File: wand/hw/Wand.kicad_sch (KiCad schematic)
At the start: 43 parts, among them J2 Conn_01x04, J2 Conn_01x08, J3 Conn_01x08, J4 Conn_01x04, M1 Motor_DC, Q1 Si2301, SW1 SW_SPST, SW2 Vib, U1 SPX3819M5-L-3-3, U2 STM32G030F6Px, U3 BMI270, U4 MMC5603NJ, U5 nRF24L01P, Y1 16MHz

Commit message: (WIP) Wand PCB design
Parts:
- added AE1: 2.4GHz 50R, Wand_footprints:ANT_IFA_USB_2.4GHz_50R, symbol Device:Antenna_Dipole
- added C19, C2: 4.7u, Capacitor_SMD:C_0603_1608Metric, symbol Device:C
- added C20: 10u, Capacitor_SMD:C_0603_1608Metric, symbol Device:C
- added D1: SMBJ5.0A, Diode_SMD:D_SMB, symbol Diode:SMF5V0A
- added D2: LED, LED_SMD:LED_0603_1608Metric, symbol Device:LED
- added J5: USB_C_Receptacle_PowerOnly_6P, Wand_footprints:USB_C_Receptacle, symbol Connector:USB_C_Receptacle_PowerOnly_6P
- added Q1: Si2301, Package_TO_SOT_SMD:SOT-23, symbol Device:Q_NMOS_GSD
- added R10, R3: 1k, Resistor_SMD:R_0603_1608Metric, symbol Device:R
- added R11, R12: 5.1k, Resistor_SMD:R_0603_1608Metric, symbol Device:R
- added R13: 2k, Resistor_SMD:R_0603_1608Metric, symbol Device:R
- added R14: 6.8k, Resistor_SMD:R_0603_1608Metric, symbol Device:R
- added U6: LTC4054ES5-4.2, Package_TO_SOT_SMD:TSOT-23-5, symbol Battery_Management:LTC4054ES5-4.2
- BT1: value LIR2016 -> LiPo
- J4: footprint Connector_PinHeader_2.00mm:PinHeader_1x04_P2.00mm_Vertical -> Connector_PinHeader_1.00mm:PinHeader_1x04_P1.00mm_Vertical
- renumbered C9 to C10, C10 to C11, C11 to C12, C12 to C13, C13 to C14, C14 to C15, C15 to C16, C16 to C17, C17 to C18, C6 to C7, C7 to C8, C8 to C9, Q1 to Q2, R6 to R7, R7 to R8, R8 to R9
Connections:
- net BMI_CS: now also U2.10 (PA3); no longer U2.14 (PA7)
- net GND: now also AE1.2, C19.2, C2.2, C20.2, D1.2 (A2), J5.A12 (GND), J5.B12 (GND), R11.2, R12.2, R13.2, U6.2 (GND)
- net MOTOR_G: now also U2.11 (PA4), R10.1; no longer Q2.1 (G), U2.16 (PA11/PA9)
- net VBAT: now also C20.1, U6.3 (BAT)
- net VDD: now also C2.1, Q1.3 (D); no longer C1.1, C1.1, C7.2, J2.1 (Pin_1), J3.1 (Pin_1), J4.2 (Pin_2), U3.5 (VDDIO), U3.8 (VDD), U4.B1 (VDD)
- net nRF_CE: now also U2.16 (PA11/PA9); no longer U2.11 (PA4)
- net nRF_CS: now also U2.14 (PA7); no longer U2.10 (PA3)
- net at C15.2, C16.1: now also AE1.1
- net SUB_VDD_G: now reaches U2.2 (PC14/PB9)
- net SUB_VDD_G: now also R3.1
- net SPI1_CK renamed SPI1_SCK
- new net: Q1.1 (G), R3.2
- new net: D2.1 (K), U6.1 (~{CHRG})
- new net: D2.2 (A), R14.2
- new net: R13.1, U6.5 (PROG)
- new net: J5.A5 (CC1), R12.1
- new net: J5.B5 (CC2), R11.1
- new net: Q2.1 (G), R10.2
- new net VBUS: C19.1, D1.1 (A1), J5.A9 (VBUS), J5.B9 (VBUS), R14.1, U6.4 (V_{CC})
- new net VDDSUB: C1.1, C1.1, C7.2, J2.1 (Pin_1), J3.1 (Pin_1), J4.2 (Pin_2), Q1.2 (S), U3.5 (VDDIO), U3.8 (VDD), U4.B1 (VDD)
- no-connect marks 10 -> 9
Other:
- note added: "LTH7"
- note added: "P1.0 1x04"
- note removed: "P2.0 1x04"
- moved on the sheet: BT1, C1, C2, C3, C7, J2, J3, J4, R1, R6, R7, R8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

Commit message: Revise wand hardware design
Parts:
- removed Q1: Si2301, Package_TO_SOT_SMD:SOT-23, symbol Device:Q_NMOS_GSD
- added Q1: Si2301, Package_TO_SOT_SMD:SOT-23, symbol Device:Q_PMOS_GSD
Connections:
- net VDD: now also Q1.2 (S)
- net VDDSUB: now also Q1.3 (D)
- net at R3.2: now also Q1.1 (G)
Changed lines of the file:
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@@
   )
   (symbol (lib_id "Wand_symbols:VDDSUB") (at 231.14 94.615 0) (unit 1)
-    (in_bom yes) (on_board yes) (dnp no) (fields_autoplaced)
+    (in_bom yes) (on_board yes) (dnp no)
     (property "Reference" "#PWR014" (at 231.14 98.425 0)
       (effects (font (size 1.27 1.27)) hide)
     )
-    (property "Value" "VDDSUB" (at 231.14 89.535 0)
+    (property "Value" "VDDSUB" (at 231.14 90.17 0)
       (effects (font (size 1.27 1.27)))
     )
@@
   )
   (symbol (lib_id "Wand_symbols:VDDSUB") (at 264.795 94.615 0) (unit 1)
-    (in_bom yes) (on_board yes) (dnp no) (fields_autoplaced)
+    (in_bom yes) (on_board yes) (dnp no)
     (property "Reference" "#PWR010" (at 264.795 98.425 0)
       (effects (font (size 1.27 1.27)) hide)
     )
-    (property "Value" "VDDSUB" (at 264.795 89.535 0)
+    (property "Value" "VDDSUB" (at 265.43 90.17 0)
       (effects (font (size 1.27 1.27)))
     )
@@
     )
   )
-  (symbol (lib_id "Device:Q_NMOS_GSD") (at 121.92 61.595 0) (unit 1)
-    (in_bom yes) (on_board yes) (dnp no)
-    (property "Reference" "Q1" (at 128.27 60.325 0)
-      (effects (font (size 1.27 1.27)) (justify left))
-    )
-    (property "Value" "Si2301" (at 128.27 62.865 0)
-      (effects (font (size 1.27 1.27)) (justify left))
-    )
-    (property "Footprint" "Package_TO_SOT_SMD:SOT-23" (at 127 59.055 0)
-      (effects (font (size 1.27 1.27)) hide)
-    )
-    (property "Datasheet" "~" (at 121.92 61.595 0)
-      (effects (font (size 1.27 1.27)) hide)
-    )
-    (pin "3")
-    (pin "1")
-    (pin "2")
-    (instances
-      (project "Wand"
-        (path "/b391cdd2-d886-4ef4-8596-8b3281b3cce1"
-          (reference "Q1") (unit 1)
-        )
-      )
-    )
-  )
   (symbol (lib_id "power:GND") (at 248.285 102.87 0) (unit 1)
     (in_bom yes) (on_board yes) (dnp no) (fields_autoplaced)
@@
   )
   (symbol (lib_id "Wand_symbols:VDDSUB") (at 186.69 34.29 0) (unit 1)
-    (in_bom yes) (on_board yes) (dnp no) (fields_autoplaced)
+    (in_bom yes) (on_board yes) (dnp no)
     (property "Reference" "#PWR023" (at 186.69 38.1 0)
       (effects (font (size 1.27 1.27)) hide)
     )
-    (property "Value" "VDDSUB" (at 186.69 29.21 0)
+    (property "Value" "VDDSUB" (at 186.69 29.845 0)
       (effects (font (size 1.27 1.27)))
     )
@@
   (symbol (lib_id "Device:Battery_Cell") (at 30.48 40.005 0) (mirror y) (unit 1)
     (in_bom yes) (on_board yes) (dnp no)
-    (property "Reference" "BT1" (at 26.67 36.8935 0)
-      (effects (font (size 1.27 1.27)) (justify left))
-    )
-    (property "Value" "LiPo" (at 26.67 39.4335 0)
+    (property "Reference" "BT1" (at 27.305 37.465 0)
+      (effects (font (size 1.27 1.27)) (justify left))
+    )
+    (property "Value" "LiPo" (at 27.305 40.005 0)
       (effects (font (size 1.27 1.27)) (justify left))
     )
@@
         )
       )
+    )
+  )
+  (symbol (lib_id "Device:Q_PMOS_GSD") (at 121.92 61.595 0) (mirror x) (unit 1)
+    (in_bom yes) (on_board yes) (dnp no)
+    (property "Reference" "Q1" (at 127.635 62.865 0)
+      (effects (font (size 1.27 1.27)) (justify left))
+    )
+    (property "Value" "Si2301" (at 127.635 60.325 0)
+      (effects (font (size 1.27 1.27)) (justify left))
+    )
+    (property "Footprint" "Package_TO_SOT_SMD:SOT-23" (at 127 64.135 0)
+      (effects (font (size 1.27 1.27)) hide)
+    )
+    (property "Datasheet" "~" (at 121.92 61.595 0)
+      (effects (font (size 1.27 1.27)) hide)
+    )
+    (pin "3")
+    (pin "1")
+    (pin "2")
+    (instances
+      (project "Wand"
+        (path "/b391cdd2-d886-4ef4-8596-8b3281b3cce1"
+          (reference "Q1") (unit 1)
+        )
+      )

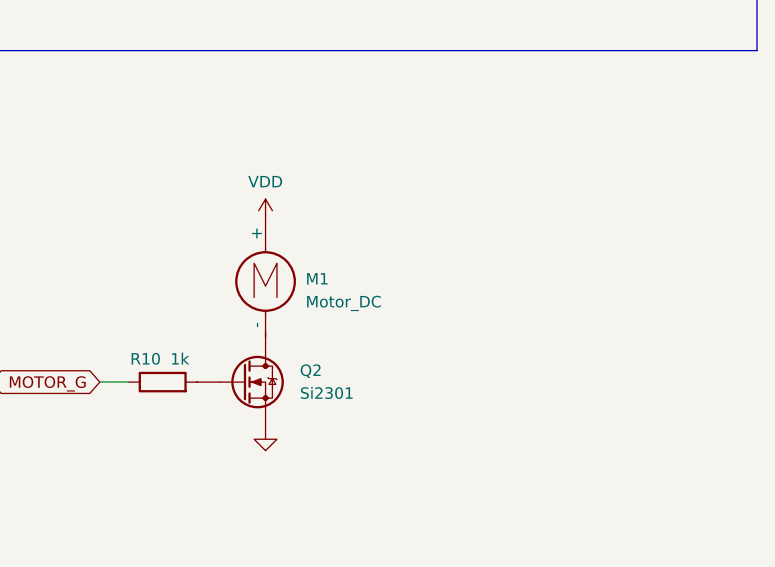
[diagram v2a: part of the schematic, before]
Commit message: Add flyback diode reminder
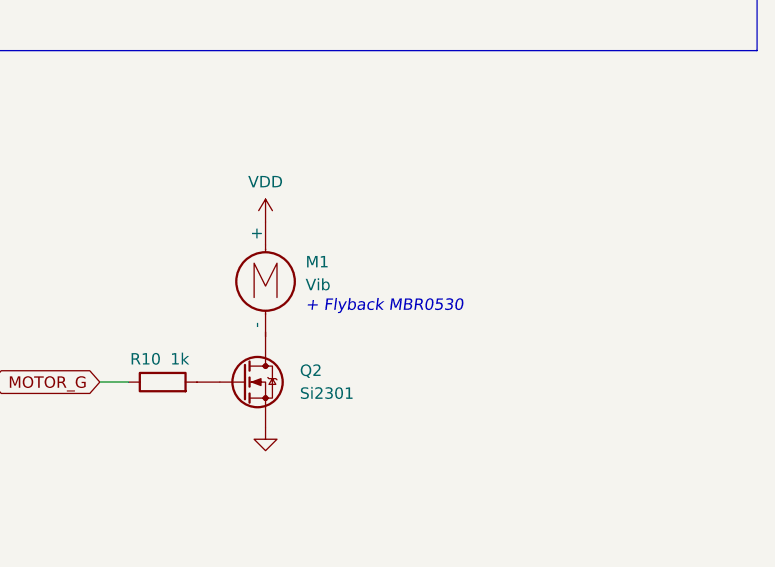
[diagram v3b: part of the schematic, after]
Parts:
- M1: value Motor_DC -> Vib
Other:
- note added: "+ Flyback MBR0530"
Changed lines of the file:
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@@
+    (effects (font (size 1.27 1.27) italic) (justify left bottom))
+  )
+  (text "+ Flyback MBR0530" (at 228.6 145.415 0)
     (effects (font (size 1.27 1.27) italic) (justify left bottom))
   )
@@
   )
   (symbol (lib_id "Motor:Motor_DC") (at 224.155 140.335 0) (unit 1)
-    (in_bom yes) (on_board yes) (dnp no) (fields_autoplaced)
-    (property "Reference" "M1" (at 228.6 141.605 0)
-      (effects (font (size 1.27 1.27)) (justify left))
-    )
-    (property "Value" "Motor_DC" (at 228.6 144.145 0)
-      (effects (font (size 1.27 1.27)) (justify left))
-    )
+    (in_bom yes) (on_board yes) (dnp no)
+    (property "Reference" "M1" (at 228.6 139.7 0)
+      (effects (font (size 1.27 1.27)) (justify left))
+    )
+    (property "Value" "Vib" (at 228.6 142.24 0)
+      (effects (font (size 1.27 1.27)) (justify left))
+    )

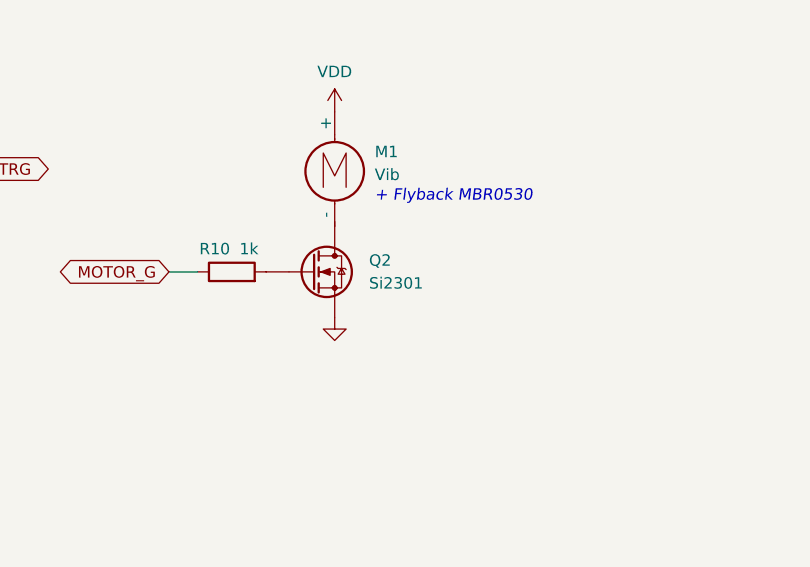
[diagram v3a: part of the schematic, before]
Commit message: Fix incorrect markings in ECAD files
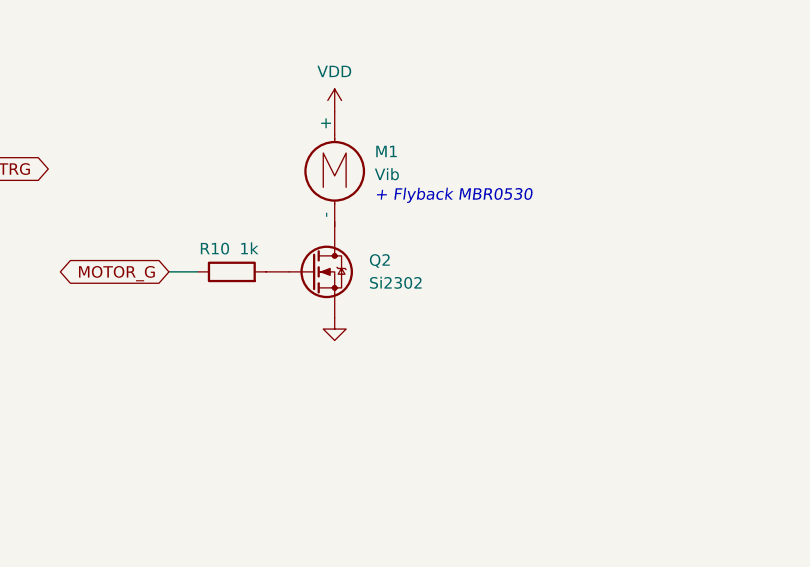
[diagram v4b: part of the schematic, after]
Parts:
- Q2: value Si2301 -> Si2302
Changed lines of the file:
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@@
       (effects (font (size 1.27 1.27)) (justify left))
     )
-    (property "Value" "Si2301" (at 227.965 154.305 0)
+    (property "Value" "Si2302" (at 227.965 154.305 0)
       (effects (font (size 1.27 1.27)) (justify left))
     )

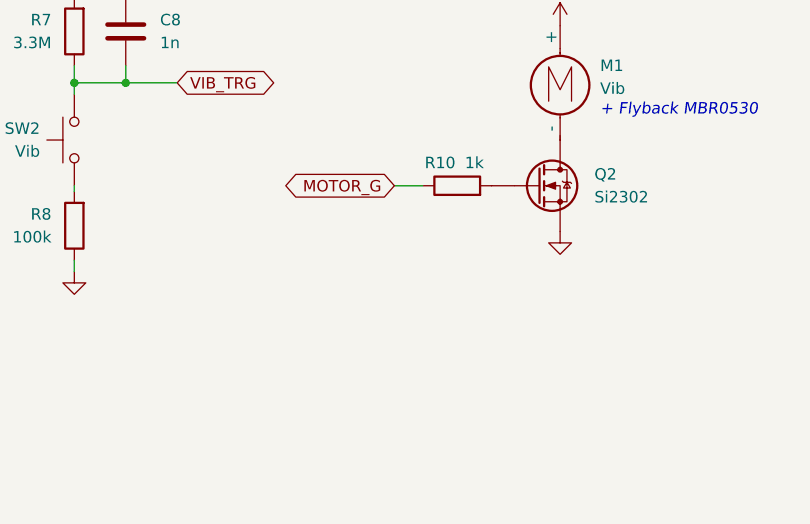
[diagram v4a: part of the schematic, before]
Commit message: Pull down motor NMOS gate for stable booting
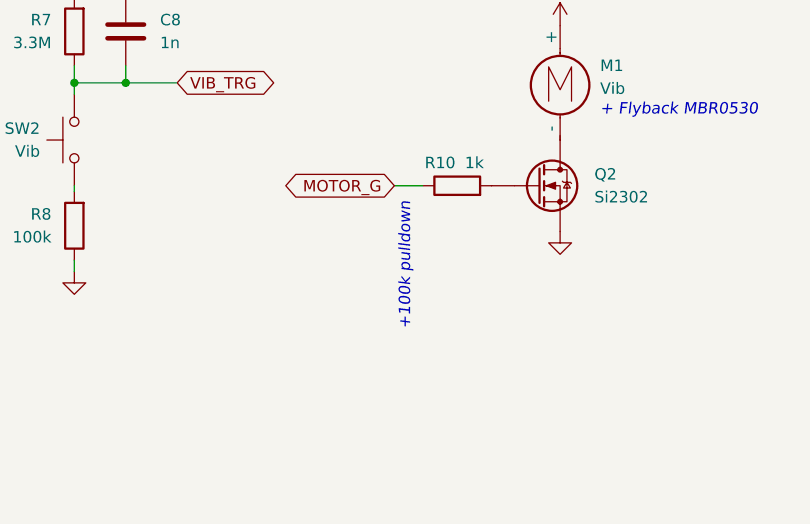
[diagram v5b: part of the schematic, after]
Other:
- note added: "+100k pulldown"
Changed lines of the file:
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@@
+    (effects (font (size 1.27 1.27) italic) (justify right bottom))
+  )
+  (text "+100k pulldown" (at 207.645 154.94 90)
     (effects (font (size 1.27 1.27) italic) (justify right bottom))
   )

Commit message: Revise wand hardware design
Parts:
- added D3: MBR0530, Diode_SMD:D_SOD-123, symbol Device:D
- added R11: 100k, Resistor_SMD:R_0603_1608Metric, symbol Device:R
- J4: footprint Connector_PinHeader_1.00mm:PinHeader_1x04_P1.00mm_Vertical -> Connector_PinHeader_1.27mm:PinHeader_1x04_P1.27mm_Vertical
- renumbered R11 to R12, R12 to R13, R13 to R14, R14 to R15
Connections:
- net GND: now also R11.1
- net MOTOR_G: now also R11.2
- net VDD: now also D3.1 (K)
- net at M1.2 (-), Q2.3 (D): now also D3.2 (A)
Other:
- note added: "P1.27 1x04"
- note removed: "+ Flyback MBR0530"
- note removed: "+100k pulldown"
- note removed: "P1.0 1x04"
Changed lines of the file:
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@@
   (junction (at 86.36 68.58) (diameter 0) (color 0 0 0 0)
   )
+  (junction (at 207.01 153.035) (diameter 0) (color 0 0 0 0)
+  )
   (junction (at 86.995 164.465) (diameter 0) (color 0 0 0 0)
   )
@@
   (junction (at 76.2 39.37) (diameter 0) (color 0 0 0 0)
   )
+  (junction (at 224.155 147.955) (diameter 0) (color 0 0 0 0)
+  )
   (junction (at 60.96 186.055) (diameter 0) (color 0 0 0 0)
   )
@@
   (junction (at 67.31 29.21) (diameter 0) (color 0 0 0 0)
   )
+  (junction (at 224.155 135.255) (diameter 0) (color 0 0 0 0)
+  )
   (junction (at 60.96 145.415) (diameter 0) (color 0 0 0 0)
   )
@@
     (stroke (width 0) (type default))
   )
-  (wire (pts (xy 205.74 153.035) (xy 208.915 153.035))
+  (wire (pts (xy 203.835 153.035) (xy 207.01 153.035))
     (stroke (width 0) (type default))
   )
@@
     (stroke (width 0) (type default))
   )
+  (wire (pts (xy 236.855 137.16) (xy 236.855 135.255))
+    (stroke (width 0) (type default))
+  )
   (wire (pts (xy 115.57 160.655) (xy 127 160.655))
     (stroke (width 0) (type default))
@@
     (stroke (width 0) (type default))
   )
+  (wire (pts (xy 236.855 147.955) (xy 224.155 147.955))
+    (stroke (width 0) (type default))
+  )
   (wire (pts (xy -15.875 27.305) (xy -13.335 27.305))
     (stroke (width 0) (type default))
@@
     (stroke (width 0) (type default))
   )
+  (wire (pts (xy 207.01 155.575) (xy 207.01 153.035))
+    (stroke (width 0) (type default))
+  )
   (wire (pts (xy 34.925 72.39) (xy 34.925 70.485))
     (stroke (width 0) (type default))
   )
+  (wire (pts (xy 236.855 135.255) (xy 224.155 135.255))
+    (stroke (width 0) (type default))
+  )
   (wire (pts (xy 36.83 173.355) (xy 36.83 178.435))
     (stroke (width 0) (type default))
@@
     (stroke (width 0) (type default))
   )
+  (wire (pts (xy 236.855 144.78) (xy 236.855 147.955))
+    (stroke (width 0) (type default))
+  )
   (wire (pts (xy 6.985 33.655) (xy 16.51 33.655))
     (stroke (width 0) (type default))
@@
     (stroke (width 0) (type default))
   )
+  (wire (pts (xy 207.01 153.035) (xy 208.915 153.035))
+    (stroke (width 0) (type default))
+  )
   (wire (pts (xy 88.9 172.085) (xy 96.52 172.085))
     (stroke (width 0) (type default))
@@
     (effects (font (size 1.27 1.27) italic) (justify right bottom))
   )
-  (text "+100k pulldown" (at 207.645 154.94 90)
-    (effects (font (size 1.27 1.27) italic) (justify right bottom))
-  )
-  (text "P1.0 1x04" (at 245.745 38.1 0)
-    (effects (font (size 1.27 1.27) italic) (justify left bottom))
-  )
-  (text "+ Flyback MBR0530" (at 228.6 145.415 0)
+  (text "P1.27 1x04" (at 245.745 38.1 0)
     (effects (font (size 1.27 1.27) italic) (justify left bottom))
   )
@@
     )
   )
-  (global_label "MOTOR_G" (shape bidirectional) (at 205.74 153.035 180) (fields_autoplaced)
+  (global_label "MOTOR_G" (shape bidirectional) (at 203.835 153.035 180) (fields_autoplaced)
     (effects (font (size 1.27 1.27)) (justify right))
-    (property "Intersheetrefs" "${INTERSHEET_REFS}" (at 193.0559 153.035 0)
+    (property "Intersheetrefs" "${INTERSHEET_REFS}" (at 191.1509 153.035 0)
       (effects (font (size 1.27 1.27)) (justify right) hide)
     )
@@
       (effects (font (size 1.27 1.27)) (justify left) hide)
     )
-    (property "Footprint" "Connector_PinHeader_1.00mm:PinHeader_1x04_P1.00mm_Vertical" (at 243.205 34.29 0)
+    (property "Footprint" "Connector_PinHeader_1.27mm:PinHeader_1x04_P1.27mm_Vertical" (at 243.205 34.29 0)
       (effects (font (size 1.27 1.27)) hide)
     )
@@
     )
   )
+  (symbol (lib_id "Device:D") (at 236.855 140.97 270) (unit 1)
+    (in_bom yes) (on_board yes) (dnp no) (fields_autoplaced)
+    (property "Reference" "D3" (at 240.03 139.7 90)
+      (effects (font (size 1.27 1.27)) (justify left))
+    )
+    (property "Value" "MBR0530" (at 240.03 142.24 90)
+      (effects (font (size 1.27 1.27)) (justify left))
+    )
+    (property "Footprint" "Diode_SMD:D_SOD-123" (at 236.855 140.97 0)
+      (effects (font (size 1.27 1.27)) hide)
+    )
+    (property "Datasheet" "~" (at 236.855 140.97 0)
+      (effects (font (size 1.27 1.27)) hide)
+    )
+    (property "Sim.Device" "D" (at 236.855 140.97 0)
+      (effects (font (size 1.27 1.27)) hide)
+    )
+    (property "Sim.Pins" "1=K 2=A" (at 236.855 140.97 0)
+      (effects (font (size 1.27 1.27)) hide)
+    )
+    (pin "2")
+    (pin "1")
+    (instances
+      (project "Wand"
+        (path "/b391cdd2-d886-4ef4-8596-8b3281b3cce1"
+          (reference "D3") (unit 1)
+        )
+      )
+    )
+  )
   (symbol (lib_id "power:GND") (at 245.745 102.87 0) (unit 1)
     (in_bom yes) (on_board yes) (dnp no) (fields_autoplaced)
@@
   (symbol (lib_id "Device:R") (at -18.415 6.35 0) (unit 1)
     (in_bom yes) (on_board yes) (dnp no)
-    (property "Reference" "R12" (at -16.51 5.08 0)
+    (property "Reference" "R13" (at -16.51 5.08 0)
       (effects (font (size 1.27 1.27)) (justify left))
     )
@@
       (project "Wand"
         (path "/b391cdd2-d886-4ef4-8596-8b3281b3cce1"
-          (reference "R12") (unit 1)
+          (reference "R13") (unit 1)
         )
       )
@@
   (symbol (lib_id "Device:R") (at -27.94 6.35 0) (unit 1)
     (in_bom yes) (on_board yes) (dnp no)
-    (property "Reference" "R11" (at -26.035 5.08 0)
+    (property "Reference" "R12" (at -26.035 5.08 0)
       (effects (font (size 1.27 1.27)) (justify left))
     )
@@
       (project "Wand"
         (path "/b391cdd2-d886-4ef4-8596-8b3281b3cce1"
-          (reference "R11") (unit 1)
+          (reference "R12") (unit 1)
         )
       )
@@
     )
   )
+  (symbol (lib_id "power:GND") (at 207.01 163.195 0) (unit 1)
+    (in_bom yes) (on_board yes) (dnp no) (fields_autoplaced)
+    (property "Reference" "#PWR019" (at 207.01 169.545 0)
+      (effects (font (size 1.27 1.27)) hide)
+    )
+    (property "Value" "GND" (at 207.01 167.64 0)
+      (effects (font (size 1.27 1.27)) hide)
+    )
+    (property "Footprint" "" (at 207.01 163.195 0)
+      (effects (font (size 1.27 1.27)) hide)
+    )
+    (property "Datasheet" "" (at 207.01 163.195 0)
+      (effects (font (size 1.27 1.27)) hide)
+    )
+    (pin "1")
+    (instances
+      (project "Wand"
+        (path "/b391cdd2-d886-4ef4-8596-8b3281b3cce1"
+          (reference "#PWR019") (unit 1)
+        )
+      )
+    )
+  )
   (symbol (lib_id "power:GND") (at 106.68 172.085 90) (unit 1)
     (in_bom yes) (on_board yes) (dnp no) (fields_autoplaced)
@@
   (symbol (lib_id "Device:R") (at -17.78 40.005 0) (mirror y) (unit 1)
     (in_bom yes) (on_board yes) (dnp no)
-    (property "Reference" "R13" (at -19.685 38.735 0)
+    (property "Reference" "R14" (at -19.685 38.735 0)
       (effects (font (size 1.27 1.27)) (justify left))
     )
@@
       (project "Wand"
         (path "/b391cdd2-d886-4ef4-8596-8b3281b3cce1"
-          (reference "R13") (unit 1)
+          (reference "R14") (unit 1)
         )
       )
@@
   (symbol (lib_id "Device:R") (at -28.575 27.305 90) (unit 1)
     (in_bom yes) (on_board yes) (dnp no)
-    (property "Reference" "R14" (at -28.575 22.225 90)
+    (property "Reference" "R15" (at -28.575 22.225 90)
       (effects (font (size 1.27 1.27)))
     )
@@
       (project "Wand"
         (path "/b391cdd2-d886-4ef4-8596-8b3281b3cce1"
-          (reference "R14") (unit 1)
+          (reference "R15") (unit 1)
         )
       )
@@
     )
   )
-  (symbol (lib_id "power:VDD") (at 224.155 135.255 0) (unit 1)
+  (symbol (lib_id "power:VDD") (at 224.155 135.255 0) (mirror y) (unit 1)
     (in_bom yes) (on_board yes) (dnp no)
     (property "Reference" "#PWR032" (at 224.155 139.065 0)
@@
         )
       )
+    )
+  )
+  (symbol (lib_id "Device:R") (at 207.01 159.385 180) (unit 1)
+    (in_bom yes) (on_board yes) (dnp no)
+    (property "Reference" "R11" (at 204.47 158.115 0)
+      (effects (font (size 1.27 1.27)) (justify left))
+    )
+    (property "Value" "100k" (at 204.47 160.655 0)
+      (effects (font (size 1.27 1.27)) (justify left))
+    )
+    (property "Footprint" "Resistor_SMD:R_0603_1608Metric" (at 208.788 159.385 90)
+      (effects (font (size 1.27 1.27)) hide)
+    )
+    (property "Datasheet" "~" (at 207.01 159.385 0)
+      (effects (font (size 1.27 1.27)) hide)
+    )
+    (pin "2")
+    (pin "1")
+    (instances
+      (project "Wand"
+        (path "/b391cdd2-d886-4ef4-8596-8b3281b3cce1"
+          (reference "R11") (unit 1)
+        )
+      )
